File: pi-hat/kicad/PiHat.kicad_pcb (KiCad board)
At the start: 2 copper layers, 49.8 x 62 mm, 10 parts, among them J1 Raspberry_Pi_2_3, J2 Power, J3 HDMI board, J4 Fan, J5 Light Panel, J6 IDC16, Q1 BD139, U1 AMZ_3A_MOD

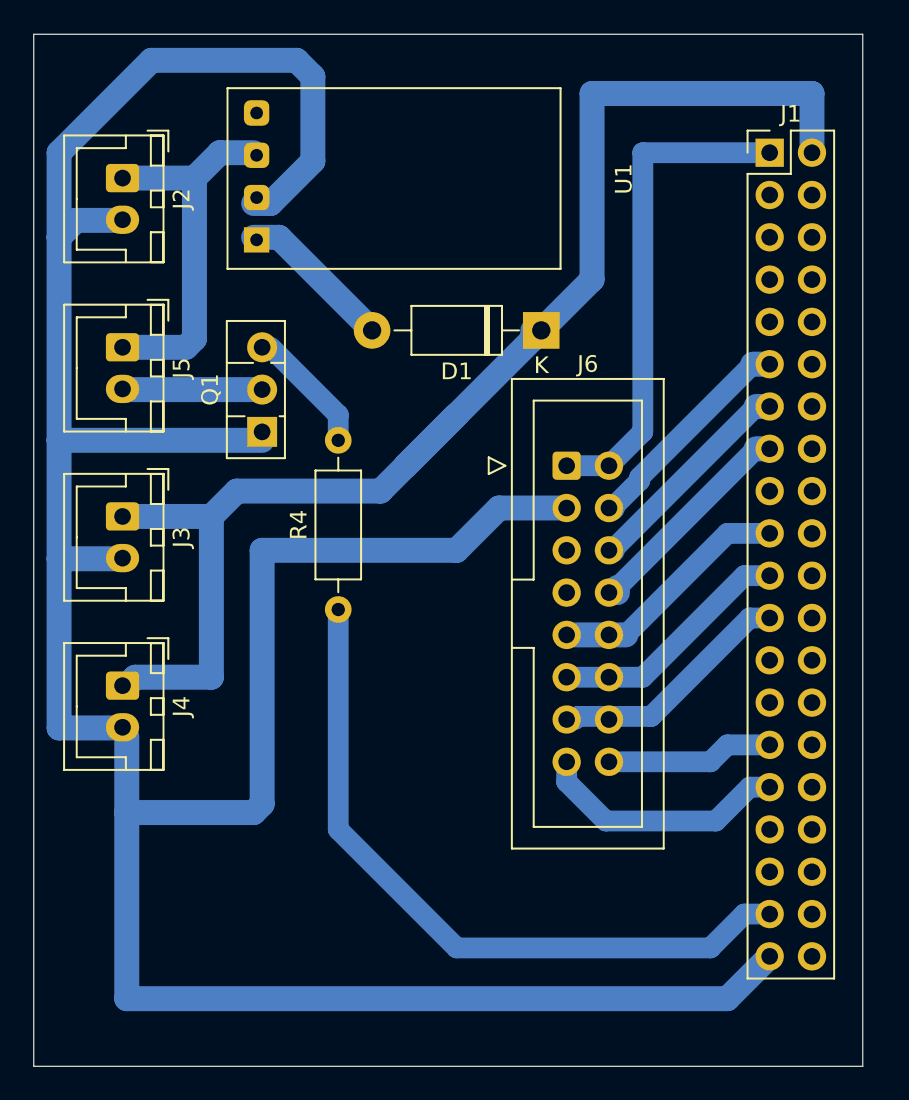
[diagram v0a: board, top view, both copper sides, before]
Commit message: Improved Gerber files for 3rd party fab
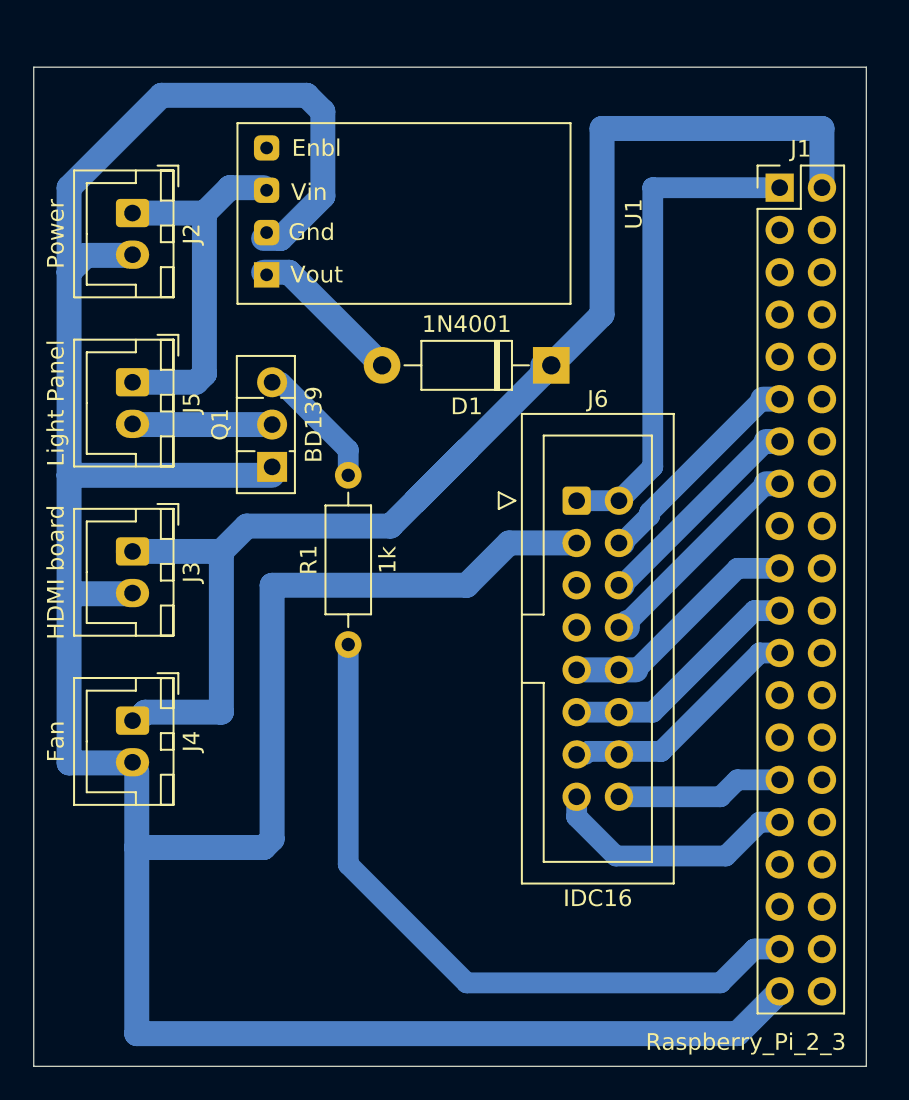
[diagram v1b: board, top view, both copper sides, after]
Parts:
- removed R4: 1k, Resistor_THT:R_Axial_DIN0207_L6.3mm_D2.5mm_P10.16mm_Horizontal
- added R1: 1k, Resistor_THT:R_Axial_DIN0207_L6.3mm_D2.5mm_P10.16mm_Horizontal, F.Cu at (29.0, 46.8)
- moved J1 2.18 mm to (55.0, 19.4)
- moved J2 2.18 mm to (16.1, 20.9)
- moved J3 2.18 mm to (16.1, 41.2)
- moved J5 2.18 mm to (16.1, 31.1)
- moved J6 2.18 mm to (42.8, 38.2)
- moved Q1 2.18 mm to (24.5, 36.1)
- moved U1 2.18 mm to (32.1, 20.9)
- moved D1 2.18 mm to (41.2, 30.0)
- moved J4 2.18 mm to (16.1, 51.4)
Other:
- board size 49.8 x 62 mm -> 50 x 60 mm

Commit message: Re-arranged PiHat pins for TFT interface board
First draft of small interface board to allow TFT screen to be connected with IDC or FFC connectors. To accommodate this, a few TFT pin assignments (Touch IRQ and Chip Select) were swapped.
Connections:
- J1 pad 13: DC -> RESET
- J1 pad 15: RESET -> DC
- J1 pad 29: T_IRQ -> T_CS
- J1 pad 31: T_CS -> T_IRQ
- J6 pad 15: T_CS -> T_IRQ
- J6 pad 16: T_IRQ -> T_CS
- J6 pad 6: DC -> RESET
- J6 pad 8: RESET -> DC
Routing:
- net T_IRQ: track 9.56 -> 15.2 mm
- net T_CS: track 15.2 -> 9.56 mm

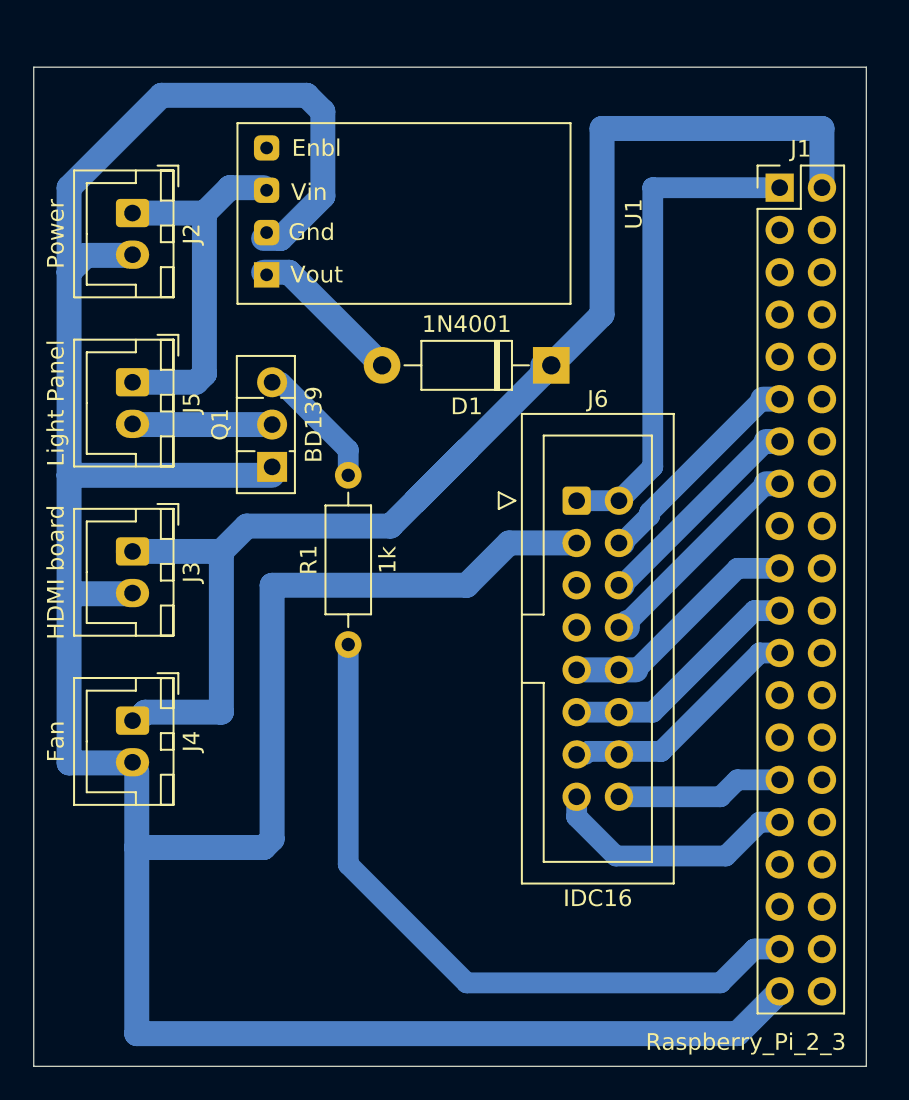
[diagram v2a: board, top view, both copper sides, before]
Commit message: Updated pi hat schematics for rev2
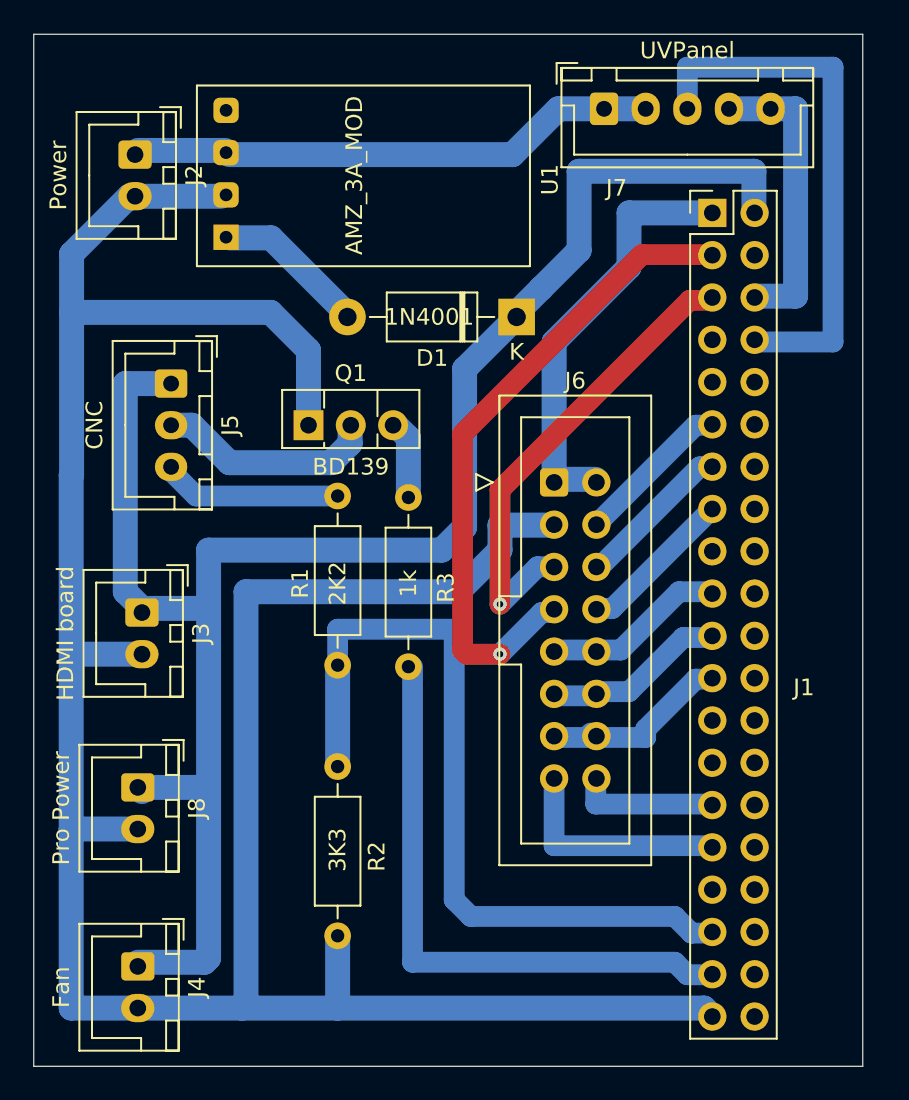
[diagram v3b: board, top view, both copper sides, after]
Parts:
- added J7: UVPanel, Connector_JST:JST_XH_B5B-XH-A_1x05_P2.50mm_Vertical, F.Cu at (44.4, 14.6)
- added J8: Pro Power, Connector_JST:JST_XH_B2B-XH-A_1x02_P2.50mm_Vertical, F.Cu at (16.4, 55.4)
- added R2: 3K3, Resistor_THT:R_Axial_DIN0207_L6.3mm_D2.5mm_P10.16mm_Horizontal, F.Cu at (28.4, 54.1)
- added R3: 1k, Resistor_THT:R_Axial_DIN0207_L6.3mm_D2.5mm_P10.16mm_Horizontal, F.Cu at (32.7, 48.1)
- J5: value Light Panel -> CNC; footprint Connector_JST:JST_XH_B2B-XH-A_1x02_P2.50mm_Vertical -> Connector_JST:JST_XH_B3B-XH-A_1x03_P2.50mm_Vertical
- R1: value 1k -> 2K2
- moved J4 14.8 mm to (16.4, 66.1)
- moved R1 8.94 mm to (28.4, 37.9), turned to 270 degrees
- moved J1 4.32 mm to (50.9, 20.9)
- moved J3 3.71 mm to (16.7, 44.9)
- moved D1 3.57 mm to (39.2, 27.1)
- moved J2 3.51 mm to (16.2, 17.4)
- moved U1 3.32 mm to (29.7, 18.6)
- moved Q1 3.32 mm to (26.7, 33.6), turned to 0 degrees
- moved J5 2.32 mm to (18.4, 31.1)
- moved J6 1.74 mm to (41.4, 37.1)
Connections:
- net BlackLightGnd renamed LaserGnd
- J1 pad 13: RESET -> DC
- J1 pad 15: DC -> RESET
- J1 pad 29: T_CS -> T_IRQ
- J1 pad 3: Net-(J1-Pad3) -> SDA
- J1 pad 31: T_IRQ -> T_CS
- J1 pad 35: Net-(J1-Pad35) -> ZProbe3V3
- J1 pad 37: LightControl -> LaserControl
- J1 pad 5: Net-(J1-Pad5) -> SCL
- J1 pad 6: Net-(J1-Pad6) -> GND
- J1 pad 8: Net-(J1-Pad8) -> UVControl
- J2 pad 1: +12V -> +24V
- J5 pad 1: +12V -> +5V
- J6 pad 15: T_IRQ -> T_CS
- J6 pad 16: T_CS -> T_IRQ
- J6 pad 5: Net-(J6-Pad5) -> SCL
- J6 pad 6: RESET -> DC
- J6 pad 7: Net-(J6-Pad7) -> SDA
- J6 pad 8: DC -> RESET
- R1 pad 1: LightControl -> ZProbeIn
- R1 pad 2: Net-(Q1-Pad3) -> ZProbe3V3
- U1 pad 3: +12V -> +24V
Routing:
- net ZProbe3V3: track 0.00 -> 47.8 mm
- net LightControl: track 42.4 -> 0.00 mm
- net SDA: track 0.00 -> 38.8 mm, vias 0 -> 1
- net LaserControl: track 0.00 -> 36.1 mm
- net UVControl: track 0.00 -> 32.5 mm
- net +24V: track 0.00 -> 31.4 mm
- net SCL: track 0.00 -> 28.0 mm, vias 0 -> 1
- net +5V: track 81.3 -> 106.7 mm
- net +12V: track 22.2 -> 0.00 mm
- net ZProbeIn: track 0.00 -> 10.6 mm
- net T_IRQ: track 15.2 -> 8.25 mm
- net GND: track 184.0 -> 189.6 mm
- net LaserGnd: track 8.64 -> 13.3 mm
- net +3V3: track 29.8 -> 25.4 mm
- net CS: track 13.3 -> 9.76 mm
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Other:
- board size 50 x 60 mm -> 49.8 x 62 mm
